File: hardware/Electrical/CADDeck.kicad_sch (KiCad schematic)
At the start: 34 parts, among them J1 Conn_01x05_Socket, J2 Conn_01x05_Pin, J3 Conn_01x04_Pin, J4 Conn_01x04_Socket, J5 Conn_01x10_Socket, J6 Conn_01x10_Pin, SW1 SW_Push, SW10 SW_Push, SW2 SW_Push, SW3 SW_Push, SW4 SW_Push, SW5 SW_Push, SW6 SW_Push, SW7 SW_Push, SW8 SW_Push, SW9 SW_Push, U1 PCF8575PWE4, U3 TTP223, U5 49E Rotate, U6 49E Zoom

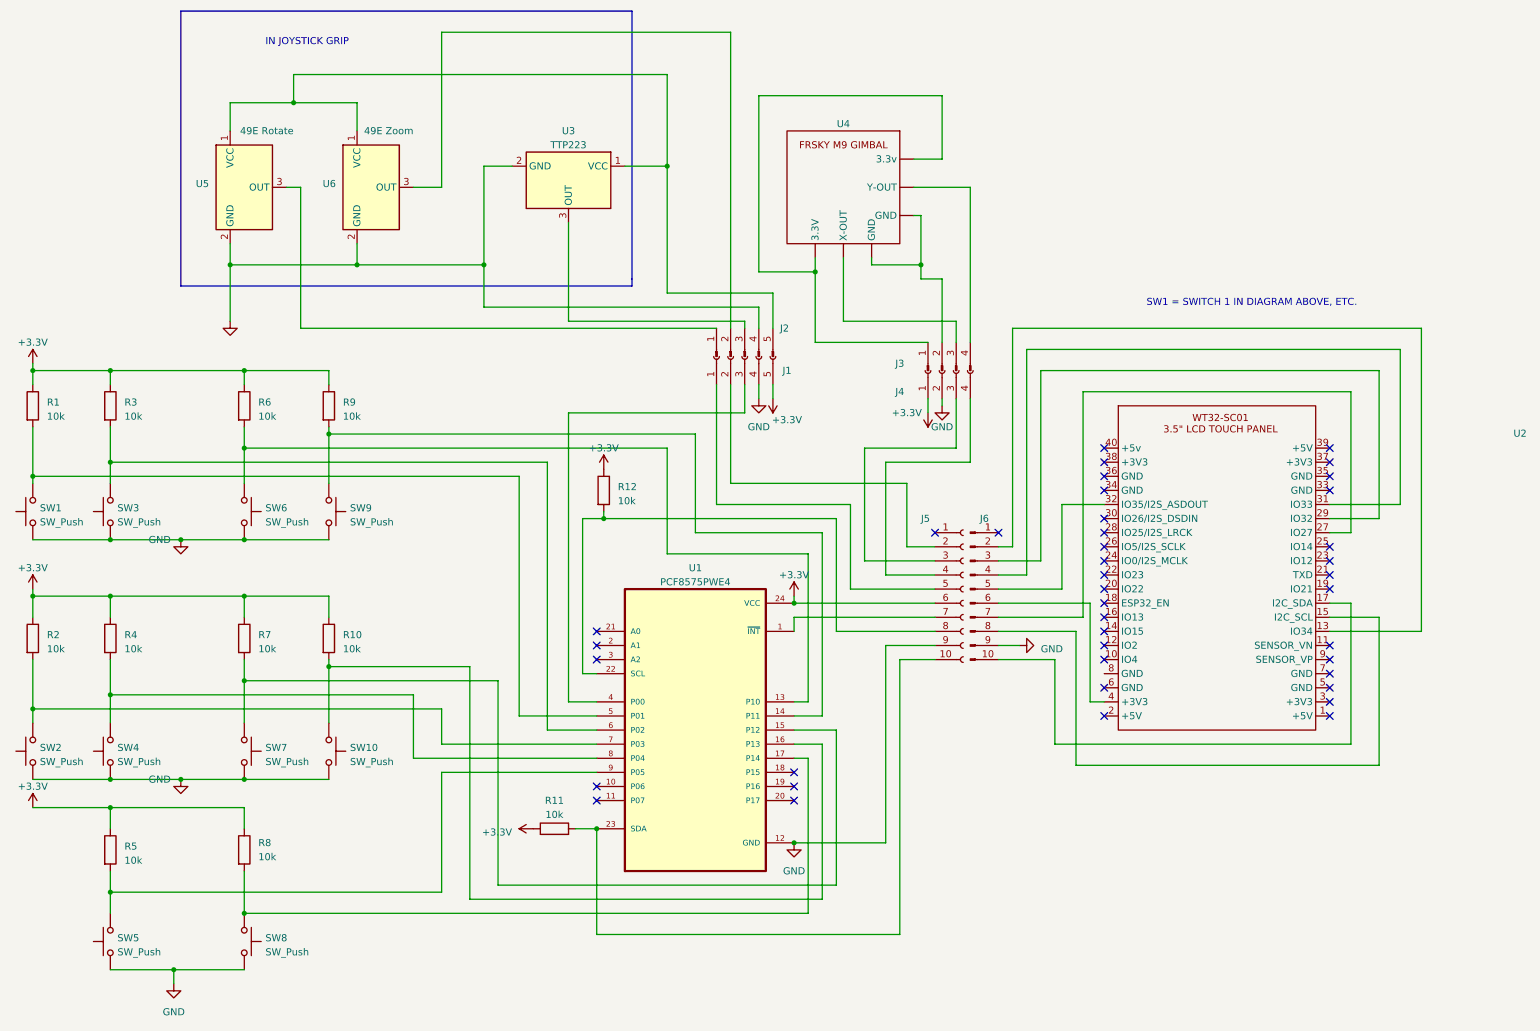
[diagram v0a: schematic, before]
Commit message: Platine aktualisiert
LED Beleuchtung für Tasten
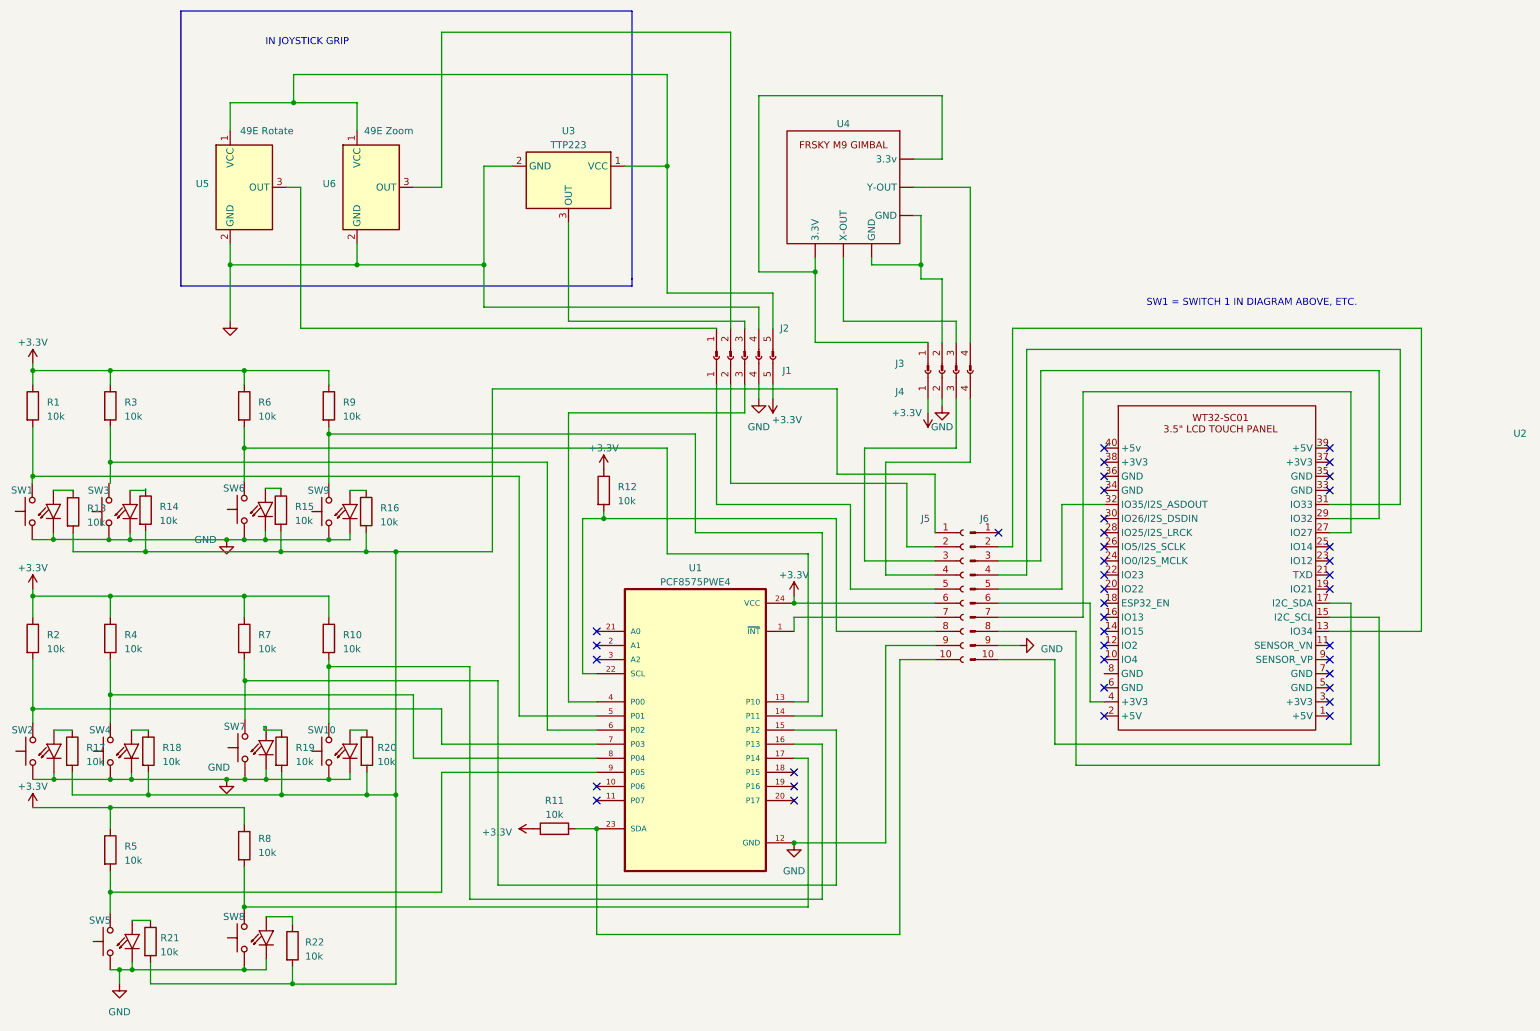
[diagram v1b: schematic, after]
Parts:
- added R13, R14, R15, R16, R17, R18, R19, R20, R21, R22: 10k, Resistor_SMD:R_0805_2012Metric_Pad1.20x1.40mm_HandSolder, symbol Device:R
- SW1, SW10, SW2, SW3, SW4, SW5, SW6, SW7, SW8, SW9: footprint Button_Switch_Keyboard:SW_Cherry_MX_1.00u_PCB -> Button_MX_LED:SW_Cherry_MX_LED_PCB
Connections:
- net GND: now also SW1.3 (Kathode_-), SW10.1, SW10.3 (Kathode_-), SW2.3 (Kathode_-), SW3.3 (Kathode_-), SW4.3 (Kathode_-), SW5.3 (Kathode_-), SW6.1, SW6.3 (Kathode_-), SW7.1, SW7.3 (Kathode_-), SW8.1, SW8.3 (Kathode_-), SW9.1, SW9.3 (Kathode_-); no longer SW10.2, SW6.2, SW7.2, SW8.2, SW9.2
- net at R6.2, U1.13 (P10): now also SW6.2; no longer SW6.1
- net at R3.2, U1.6 (P02): no longer SW3.2
- net at R8.2, U1.17 (P14): now also SW8.2; no longer SW8.1
- net at R7.2, U1.15 (P12): now also SW7.2; no longer SW7.1
- net at R10.2, U1.16 (P13): now also SW10.2; no longer SW10.1
- net at R9.2, U1.14 (P11): now also SW9.2; no longer SW9.1
- net at J5.1 (Pin_1): now also R13.2, R14.2, R15.2, R16.2, R17.2, R18.2, R19.2, R20.2, R22.2
- new net: R13.1, SW1.4 (Anode_+)
- new net: R20.1, SW10.4 (Anode_+)
- new net: R22.1, SW8.4 (Anode_+)
- new net: R16.1, SW9.4 (Anode_+)
- new net: R17.1, SW2.4 (Anode_+)
- new net: R19.1, SW7.4 (Anode_+)
- new net: R15.1, SW6.4 (Anode_+)
- new net: R21.1, SW5.4 (Anode_+)
- new net: R18.1, SW4.4 (Anode_+)
- new net: R14.1, SW3.4 (Anode_+)
- no-connect marks 41 -> 40
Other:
- moved on the sheet: R8

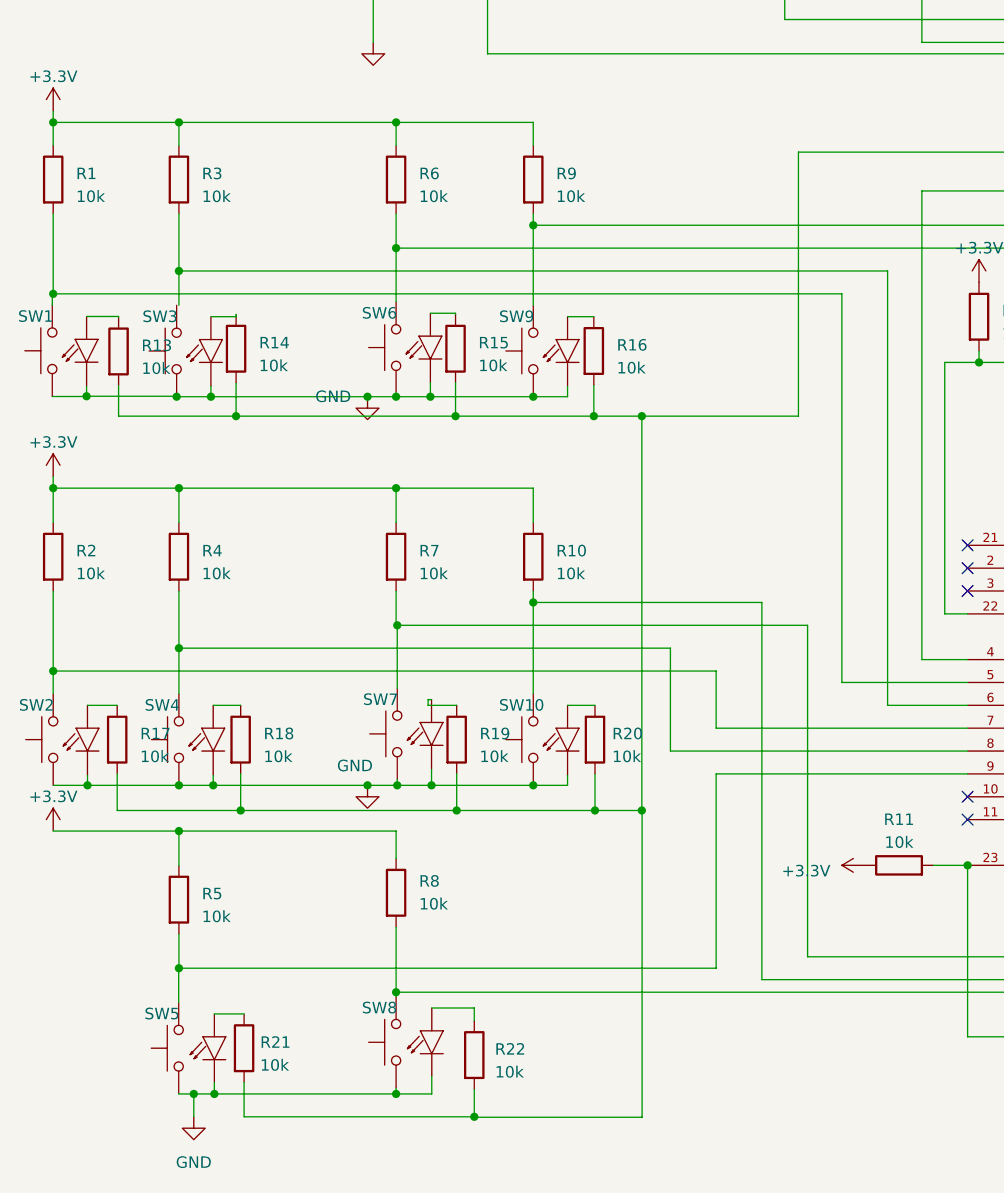
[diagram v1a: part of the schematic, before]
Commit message: Platine Fehler beseitigt
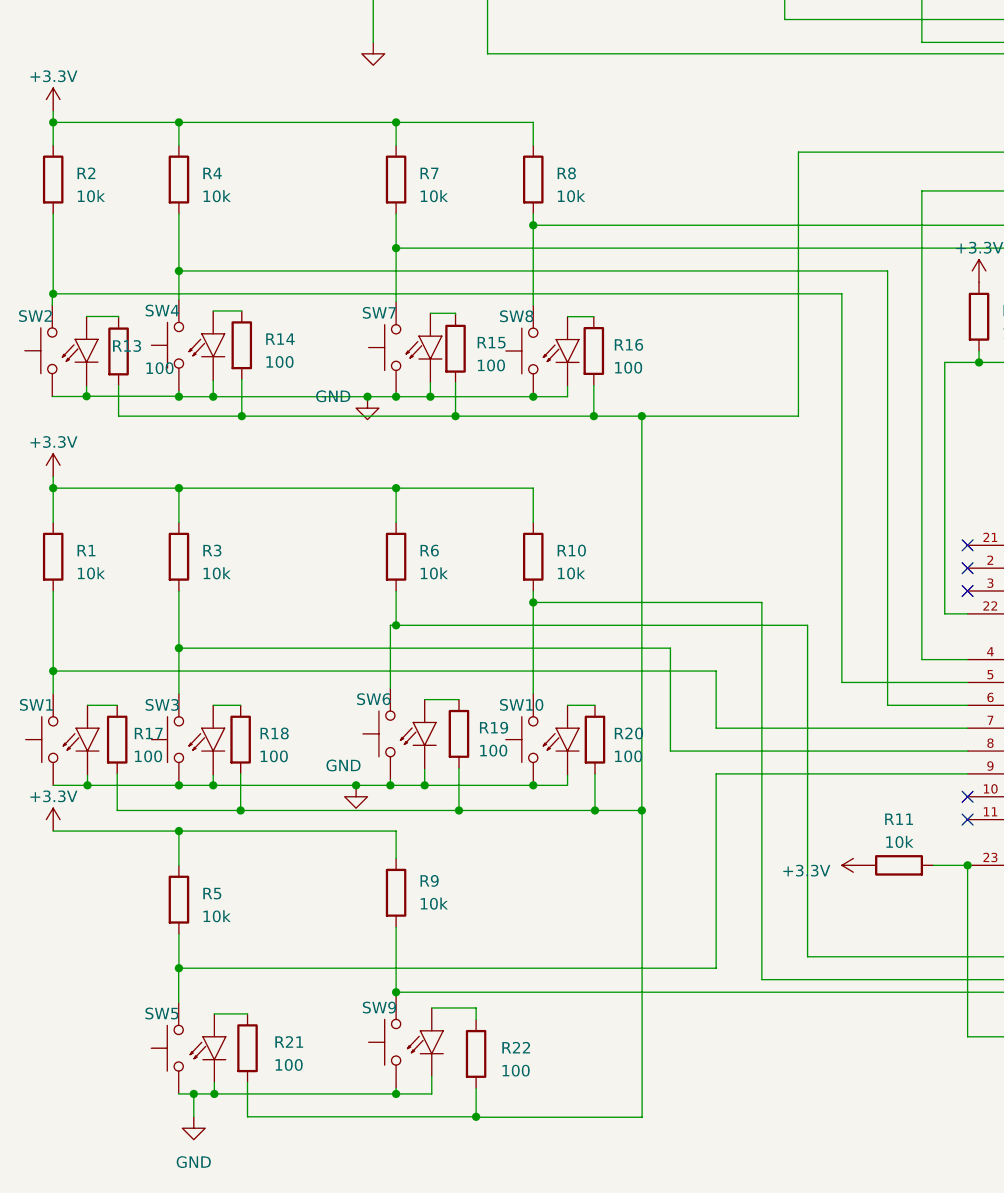
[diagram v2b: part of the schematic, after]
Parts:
- R13, R14, R15, R16, R17, R18, R19, R20, R21, R22: value 10k -> 100
- renumbered R2 to R1, R1 to R2, R4 to R3, R3 to R4, R7 to R6, R6 to R7, R9 to R8, R8 to R9, SW2 to SW1, SW1 to SW2, SW4 to SW3, SW3 to SW4, SW7 to SW6, SW6 to SW7, SW9 to SW8, SW8 to SW9
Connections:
- net at J5.1 (Pin_1), R13.2, R14.2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: now also R21.2
- net at R4.2, U1.6 (P02): now also SW4.2
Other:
- moved on the sheet: R14, R19, SW4, SW6

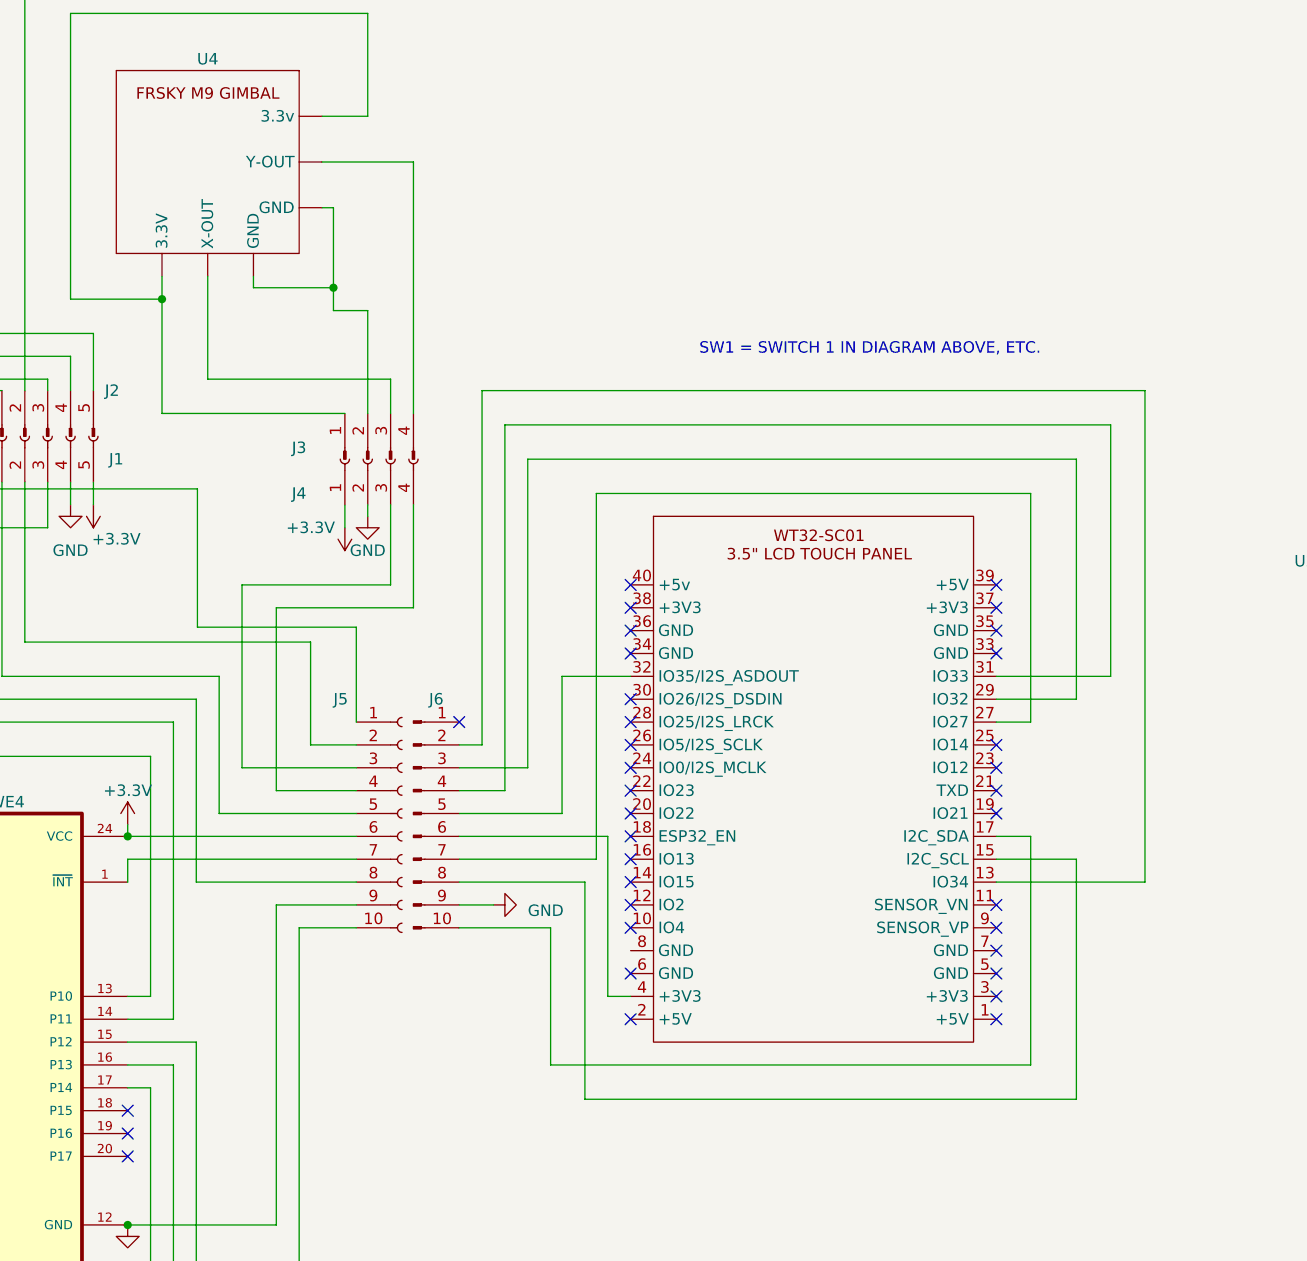
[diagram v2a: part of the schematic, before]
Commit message: MX_LED_Beleuchtung hinzugefügt
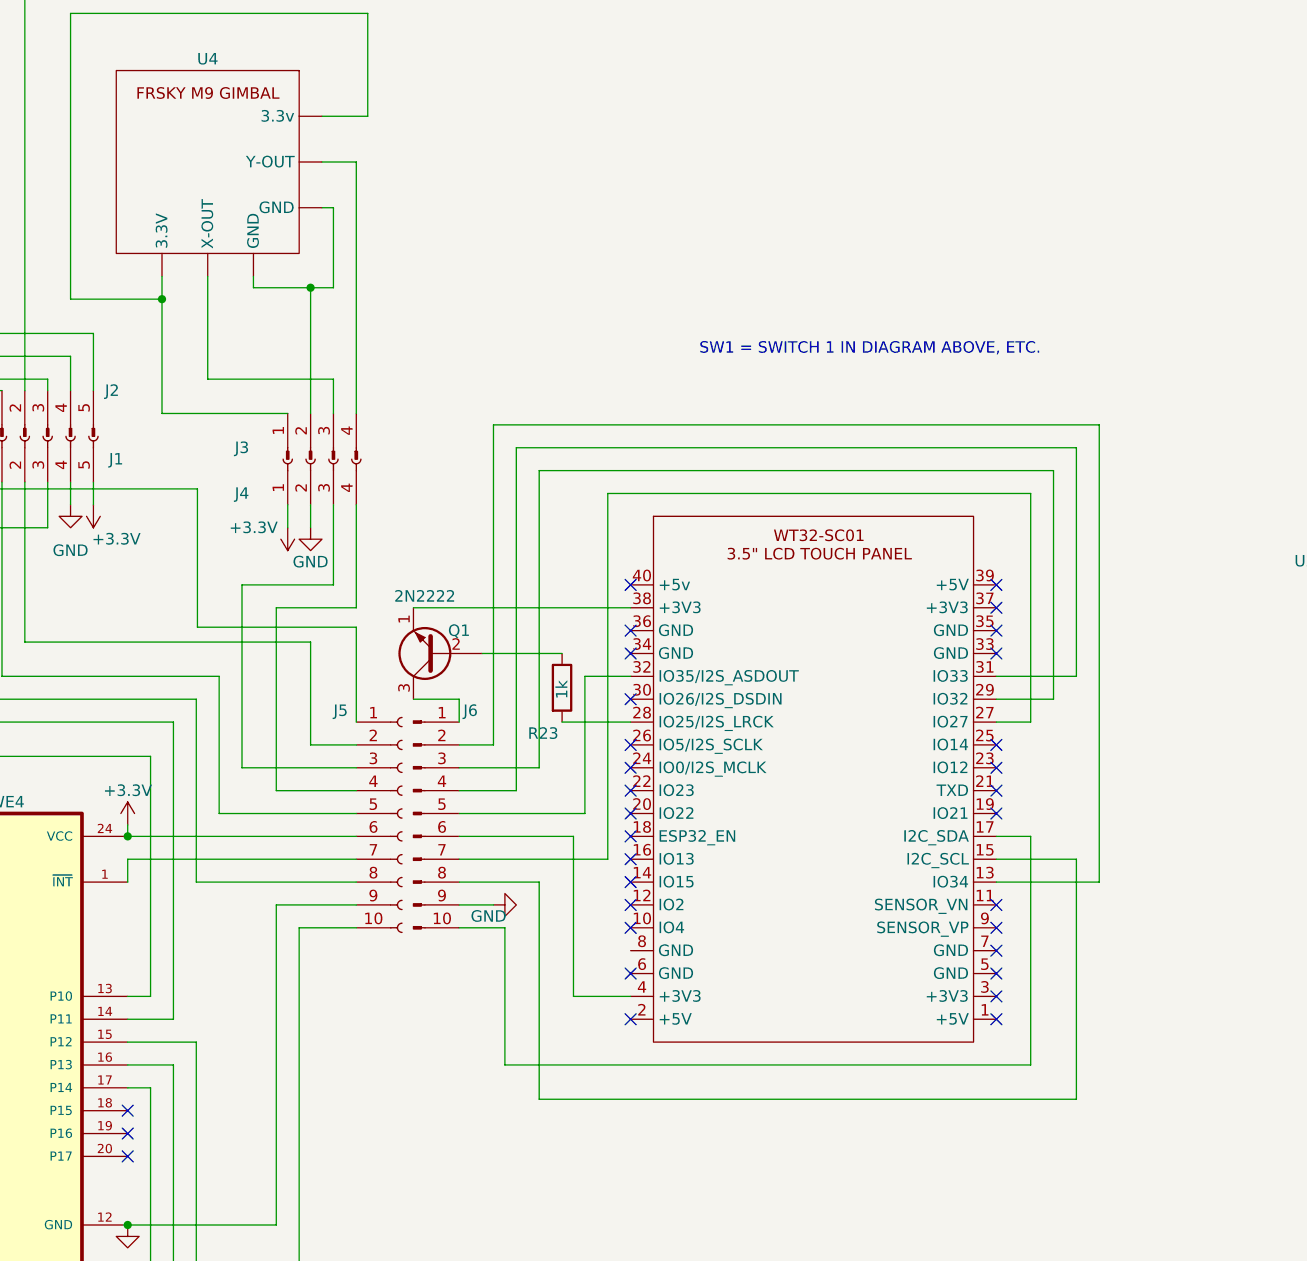
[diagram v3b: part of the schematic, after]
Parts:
- added Q1: 2N2222, Package_TO_SOT_THT:TO-39-3, symbol Transistor_BJT:2N2219
- added R23: 1k, symbol Device:R
- SW1, SW10, SW2, SW3, SW4, SW5, SW6, SW7, SW8, SW9: footprint Button_MX_LED:SW_Cherry_MX_LED_PCB -> Cherry_MX_LED:Cherry_MX_LED
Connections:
- net at J6.1 (Pin_1): now also Q1.3 (C)
- net at U2.28 (IO25/I2S_LRCK): now also R23.2
- net at U2.38 (+3V3): now also Q1.1 (E)
- new net: Q1.2 (B), R23.1
- no-connect marks 40 -> 37
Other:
- moved on the sheet: J3, J4
